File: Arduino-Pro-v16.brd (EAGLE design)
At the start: 100 x 80 mm, 41 parts, among them IC1 ATMEGA1281-16AU

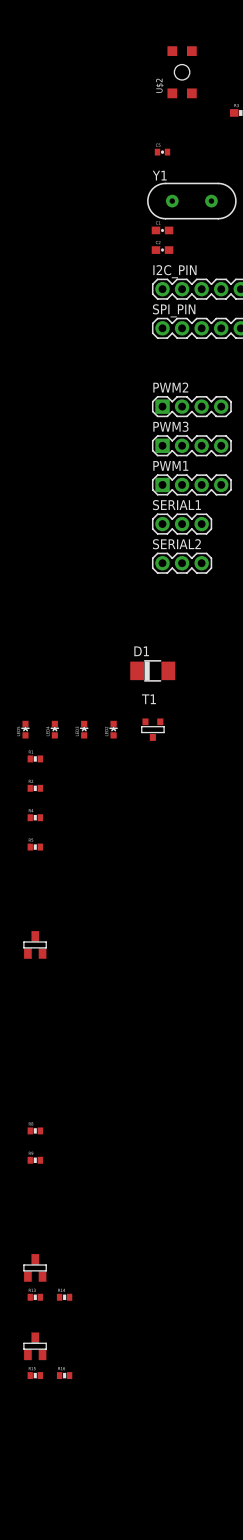
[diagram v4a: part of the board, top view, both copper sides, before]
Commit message: Added JTAG pins and smaller pushbutton
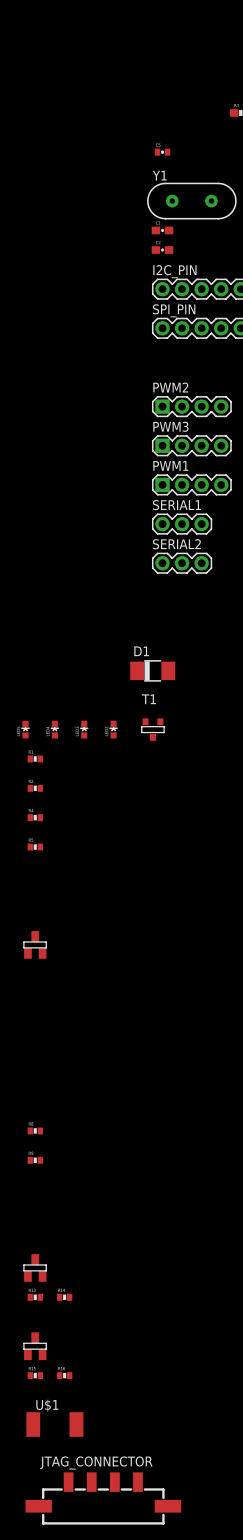
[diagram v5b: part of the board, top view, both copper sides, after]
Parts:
- removed U$2: TACTILE-SWITCH-7914G, GeekAmmo:7914G
- added JTAG_CONNECTOR: MICRO-FIT-4-SMD-PART, Connectors:MICRO-FIT-4-SMD
- added U$1: SWITCH, DiscreteComponents:SW_2512
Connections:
- new net JTTCK: IC1.57, JTAG_CONNECTOR.C4
- new net JTTDI: IC1.54, JTAG_CONNECTOR.C1
- new net JTTDO: IC1.55, JTAG_CONNECTOR.C2
- new net JTTMS: IC1.56, JTAG_CONNECTOR.C3
- net GND: now also U$1.1; no longer U$2.1, U$2.2
- net RESET: now also U$1.2; no longer U$2.3, U$2.4
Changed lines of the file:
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@@
 <?xml version="1.0" encoding="utf-8"?>
 <!DOCTYPE eagle SYSTEM "eagle.dtd">
-<eagle version="7.3.0">
+<eagle version="7.6.0">
 <drawing>
 <settings>
@@
 <element name="C5" library="SparkFun" package="0402-CAP" value="0.1uF" x="-55.88" y="-113.03"/>
 <element name="R3" library="SparkFun-Passives" package="0603-RES" value="10K" x="-45.72" y="-107.95"/>
-<element name="U$2" library="GeekAmmo" package="7914G" value="TACTILE-SWITCH-7914G" x="-54.61" y="-105.41"/>
 <element name="Y1" library="SparkFun-FreqCtrl" package="HC49US" value="" x="-52.07" y="-119.38"/>
 <element name="C1" library="SparkFun-Capacitors" package="0603-CAP" value="" x="-55.88" y="-123.19"/>
@@
 <element name="R15" library="SparkFun" package="0402-RES" value="10K" x="-72.39" y="-271.78"/>
 <element name="R16" library="SparkFun" package="0402-RES" value="10K" x="-68.58" y="-271.78"/>
+<element name="U$1" library="DiscreteComponents" package="SW_2512" value="SWITCH" x="-69.85" y="-278.13"/>
+<element name="JTAG_CONNECTOR" library="Connectors" package="MICRO-FIT-4-SMD" value="MICRO-FIT-4-SMD-PART" x="-73.66" y="-289.56">
+<attribute name="DIGIKEY-FEMALE-PN" value="WM2640CT-ND" x="-73.66" y="-289.56" size="1.778" layer="27" display="off"/>
+<attribute name="DIGIKEY-CONTACT-PN" value="WM1125CT-ND" x="-73.66" y="-289.56" size="1.778" layer="27" display="off"/>
+<attribute name="DIGIKEY-MALE-PN" value="WM1847-ND" x="-73.66" y="-289.56" size="1.778" layer="27" display="off"/>
+</element>
 </elements>
 <signals>
@@
 <contactref element="IC1" pad="22"/>
 <contactref element="C5" pad="1"/>
-<contactref element="U$2" pad="1"/>
-<contactref element="U$2" pad="2"/>
 <contactref element="IC1" pad="53"/>
 <contactref element="IC1" pad="63"/>
@@
 <contactref element="PCB1" pad="P$39"/>
 <contactref element="PCB1" pad="P$9"/>
+<contactref element="U$1" pad="1"/>
 <wire x1="-50.8" y1="-161.29" x2="-50.8" y2="-166.37" width="0" layer="19" extent="1-1"/>
 <wire x1="-45.72" y1="-135.89" x2="-50.8" y2="-161.29" width="0" layer="19" extent="1-1"/>
@@
 <wire x1="-55.03" y1="-123.19" x2="-55.03" y2="-125.73" width="0" layer="19" extent="1-1"/>
 <wire x1="-56.53" y1="-113.03" x2="-55.03" y2="-123.19" width="0" layer="19" extent="1-1"/>
-<wire x1="-54.61" y1="-105.41" x2="-56.53" y2="-113.03" width="0" layer="19" extent="1-1"/>
-<wire x1="-54.61" y1="-99.9236" x2="-54.61" y2="-105.41" width="0" layer="19" extent="1-1"/>
-<wire x1="-51.4985" y1="-89.0397" x2="-54.61" y2="-99.9236" width="0" layer="19" extent="1-1"/>
+<wire x1="-51.4985" y1="-89.0397" x2="-56.53" y2="-113.03" width="0" layer="19" extent="1-1"/>
 <wire x1="-54.6481" y1="-73.5203" x2="-51.4985" y2="-89.0397" width="0" layer="19" extent="1-1"/>
 <wire x1="-46.7741" y1="-73.5203" x2="-54.6481" y2="-73.5203" width="0" layer="19" extent="1-1"/>
@@
 <wire x1="-73.04" y1="-199.39" x2="-73.04" y2="-195.58" width="0" layer="19" extent="1-1"/>
 <wire x1="-73.04" y1="-203.2" x2="-73.04" y2="-199.39" width="0" layer="19" extent="1-1"/>
+<wire x1="-72.65" y1="-278.13" x2="-73.04" y2="-203.2" width="0" layer="19" extent="1-1"/>
 <wire x1="-13.2334" y1="-5.9182" x2="-46.7741" y2="-73.5203" width="0" layer="19" extent="1-1"/>
 <wire x1="-18.3134" y1="-3.3782" x2="-13.2334" y2="-5.9182" width="0" layer="19" extent="1-1"/>
@@
 <signal name="RESET">
 <contactref element="JP3" pad="5"/>
-<contactref element="U$2" pad="3"/>
-<contactref element="U$2" pad="4"/>
 <contactref element="R3" pad="1"/>
 <contactref element="IC1" pad="20"/>
-<wire x1="-52.07" y1="-99.9236" x2="-52.07" y2="-105.41" width="0" layer="19" extent="1-1"/>
-<wire x1="-46.57" y1="-107.95" x2="-52.07" y2="-105.41" width="0" layer="19" extent="1-1"/>
-<wire x1="-53.0733" y1="-89.0397" x2="-52.07" y2="-99.9236" width="0" layer="19" extent="1-1"/>
+<contactref element="U$1" pad="2"/>
+<wire x1="-53.0733" y1="-89.0397" x2="-46.57" y2="-107.95" width="0" layer="19" extent="1-1"/>
 <wire x1="-25.4" y1="3.81" x2="-53.0733" y2="-89.0397" width="0" layer="19" extent="1-1"/>
+<wire x1="-67.05" y1="-278.13" x2="-46.57" y2="-107.95" width="0" layer="19" extent="1-1"/>
 </signal>
 <signal name="SCK">
@@
 <wire x1="-20.8534" y1="-3.3782" x2="-23.3934" y2="-3.3782" width="0" layer="19" extent="1-1"/>
 </signal>
+<signal name="JTTDI">
+<contactref element="IC1" pad="54"/>
+<contactref element="JTAG_CONNECTOR" pad="C1"/>
+<wire x1="-68.06" y1="-285.605" x2="-47.5615" y2="-73.5203" width="0" layer="19" extent="1-1"/>
+</signal>
+<signal name="JTTDO">
+<contactref element="IC1" pad="55"/>
+<contactref element="JTAG_CONNECTOR" pad="C2"/>
+<wire x1="-65.06" y1="-285.605" x2="-48.3489" y2="-73.5203" width="0" layer="19" extent="1-1"/>
+</signal>
+<signal name="JTTMS">
+<contactref element="IC1" pad="56"/>
+<contactref element="JTAG_CONNECTOR" pad="C3"/>
+<wire x1="-62.06" y1="-285.605" x2="-49.1363" y2="-73.5203" width="0" layer="19" extent="1-1"/>
+</signal>
+<signal name="JTTCK">
+<contactref element="IC1" pad="57"/>
+<contactref element="JTAG_CONNECTOR" pad="C4"/>
+<wire x1="-59.06" y1="-285.605" x2="-49.9237" y2="-73.5203" width="0" layer="19" extent="1-1"/>
+</signal>
 </signals>

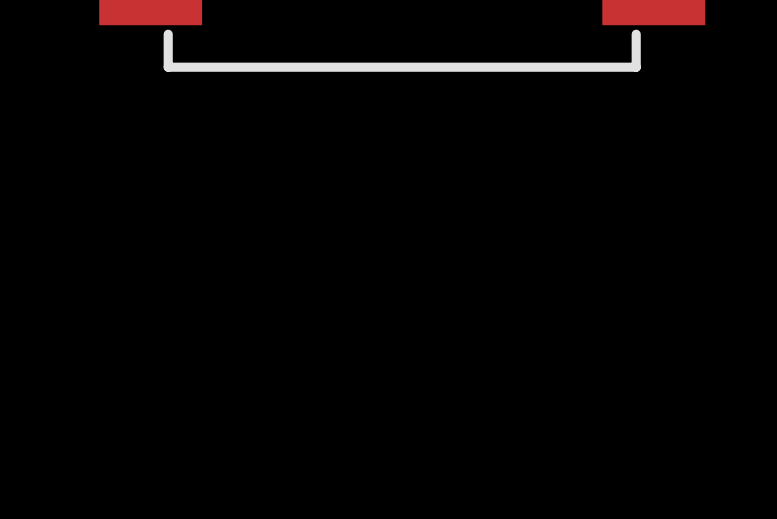
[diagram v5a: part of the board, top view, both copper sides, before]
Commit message: Added FTDI 3.3V programmer
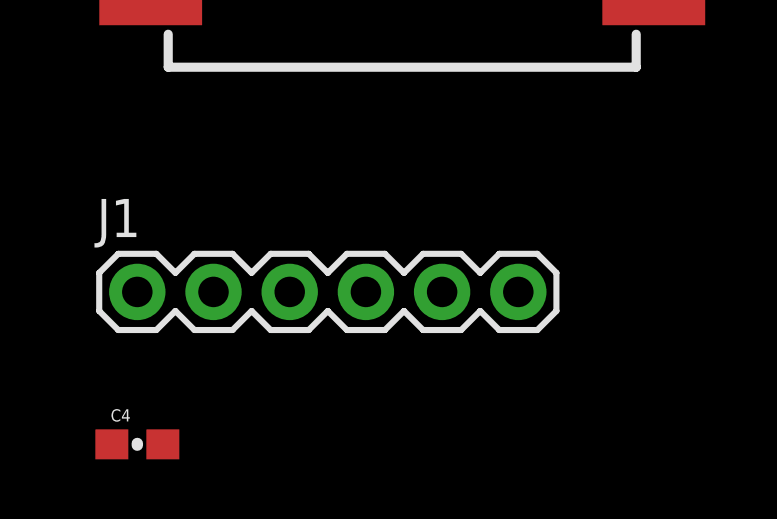
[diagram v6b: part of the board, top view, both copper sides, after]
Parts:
- added C4: (no value), SparkFun-Capacitors:0603-CAP
- added J1: FTDI Basic Programmer, SparkFun-Connectors:1X06
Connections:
- removed net VCCA: PCB1.P$2, PCB1.P$4
- new net DTR: C4.2, J1.1
- new net RXI: IC1.27, J1.3
- new net TX0: IC1.28, J1.2
- net 3V3: now also J1.4, PCB1.P$1, PCB1.P$17
- net 5VMISO: now also JP3.1
- net 5VMOSI: now also JP3.4
- net 5VROV: now also PCB1.P$2, PCB1.P$4
- net 5VSCK: now also JP3.3
- net GND: now also J1.5, J1.6
- net MISO: no longer JP3.1
- net MOSI: no longer JP3.4
- net RESET: now also C4.1
- net SCK: no longer JP3.3
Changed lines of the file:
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@@
 <attribute name="DIGIKEY-MALE-PN" value="WM1847-ND" x="-73.66" y="-289.56" size="1.778" layer="27" display="off"/>
 </element>
+<element name="J1" library="SparkFun-Connectors" package="1X06" value="FTDI Basic Programmer" x="-72.39" y="-298.45"/>
+<element name="C4" library="SparkFun-Capacitors" package="0603-CAP" value="" x="-72.39" y="-303.53"/>
 </elements>
 <signals>
@@
 <contactref element="PCB1" pad="P$9"/>
 <contactref element="U$1" pad="1"/>
+<contactref element="J1" pad="6"/>
+<contactref element="J1" pad="5"/>
 <wire x1="-50.8" y1="-161.29" x2="-50.8" y2="-166.37" width="0" layer="19" extent="1-1"/>
 <wire x1="-45.72" y1="-135.89" x2="-50.8" y2="-161.29" width="0" layer="19" extent="1-1"/>
@@
 <wire x1="-73.04" y1="-203.2" x2="-73.04" y2="-199.39" width="0" layer="19" extent="1-1"/>
 <wire x1="-72.65" y1="-278.13" x2="-73.04" y2="-203.2" width="0" layer="19" extent="1-1"/>
+<wire x1="-62.23" y1="-298.45" x2="-72.65" y2="-278.13" width="0" layer="19" extent="1-1"/>
+<wire x1="-59.69" y1="-298.45" x2="-62.23" y2="-298.45" width="0" layer="19" extent="1-1"/>
 <wire x1="-13.2334" y1="-5.9182" x2="-46.7741" y2="-73.5203" width="0" layer="19" extent="1-1"/>
 <wire x1="-18.3134" y1="-3.3782" x2="-13.2334" y2="-5.9182" width="0" layer="19" extent="1-1"/>
@@
 <contactref element="IC1" pad="20"/>
 <contactref element="U$1" pad="2"/>
+<contactref element="C4" pad="1"/>
 <wire x1="-53.0733" y1="-89.0397" x2="-46.57" y2="-107.95" width="0" layer="19" extent="1-1"/>
 <wire x1="-25.4" y1="3.81" x2="-53.0733" y2="-89.0397" width="0" layer="19" extent="1-1"/>
 <wire x1="-67.05" y1="-278.13" x2="-46.57" y2="-107.95" width="0" layer="19" extent="1-1"/>
+<wire x1="-73.24" y1="-303.53" x2="-67.05" y2="-278.13" width="0" layer="19" extent="1-1"/>
 </signal>
 <signal name="SCK">
-<contactref element="JP3" pad="3"/>
 <contactref element="SPI_PIN" pad="4"/>
-<wire x1="-27.94" y1="3.81" x2="-48.26" y2="-135.89" width="0" layer="19" extent="1-1"/>
 </signal>
 <signal name="N$38">
@@
 </signal>
 <signal name="MISO">
-<contactref element="JP3" pad="1"/>
 <contactref element="SPI_PIN" pad="2"/>
-<wire x1="-30.48" y1="3.81" x2="-53.34" y2="-135.89" width="0" layer="19" extent="1-1"/>
 </signal>
 <signal name="MOSI">
-<contactref element="JP3" pad="4"/>
 <contactref element="SPI_PIN" pad="3"/>
-<wire x1="-27.94" y1="6.35" x2="-50.8" y2="-135.89" width="0" layer="19" extent="1-1"/>
 </signal>
 <signal name="VCC">
@@
 <contactref element="D1" pad="A"/>
 <contactref element="T1" pad="3"/>
+<contactref element="PCB1" pad="P$2"/>
+<contactref element="PCB1" pad="P$4"/>
 <wire x1="-55.125" y1="-180.34" x2="-56.1594" y2="-186.944" width="0" layer="19" extent="1-1"/>
+<wire x1="-23.3934" y1="-3.3782" x2="-55.125" y2="-180.34" width="0" layer="19" extent="1-1"/>
+<wire x1="-20.8534" y1="-3.3782" x2="-23.3934" y2="-3.3782" width="0" layer="19" extent="1-1"/>
 </signal>
 <signal name="5VPROGRAMMER">
@@
 <contactref element="U$4" pad="2"/>
 <contactref element="IC1" pad="12"/>
+<contactref element="JP3" pad="4"/>
+<wire x1="-27.94" y1="6.35" x2="-57.2897" y2="-84.0359" width="0" layer="19" extent="1-1"/>
 <wire x1="-71.44" y1="-258.91" x2="-57.2897" y2="-84.0359" width="0" layer="19" extent="1-1"/>
 <wire x1="-69.23" y1="-261.62" x2="-71.44" y2="-258.91" width="0" layer="19" extent="1-1"/>
@@
 <contactref element="R13" pad="2"/>
 <contactref element="U$4" pad="1"/>
+<contactref element="PCB1" pad="P$1"/>
+<contactref element="PCB1" pad="P$17"/>
+<contactref element="J1" pad="4"/>
+<wire x1="-71.74" y1="-271.78" x2="-64.77" y2="-298.45" width="0" layer="19" extent="1-1"/>
 <wire x1="-72.39" y1="-266.87" x2="-71.74" y2="-271.78" width="0" layer="19" extent="1-1"/>
 <wire x1="-71.74" y1="-261.62" x2="-72.39" y2="-266.87" width="0" layer="19" extent="1-1"/>
@@
 <wire x1="-71.74" y1="-240.03" x2="-72.39" y2="-256.71" width="0" layer="19" extent="1-1"/>
 <wire x1="-72.39" y1="-214.8" x2="-71.74" y2="-240.03" width="0" layer="19" extent="1-1"/>
+<wire x1="-23.38" y1="-5.92" x2="-72.39" y2="-214.8" width="0" layer="19" extent="1-1"/>
+<wire x1="-3.0734" y1="-5.9182" x2="-23.38" y2="-5.92" width="0" layer="19" extent="1-1"/>
 </signal>
 <signal name="3V3MOSI">
@@
 <contactref element="U$3" pad="2"/>
 <contactref element="IC1" pad="13"/>
+<contactref element="JP3" pad="1"/>
+<wire x1="-30.48" y1="3.81" x2="-57.2897" y2="-84.8233" width="0" layer="19" extent="1-1"/>
 <wire x1="-71.44" y1="-217" x2="-57.2897" y2="-84.8233" width="0" layer="19" extent="1-1"/>
 <wire x1="-73.04" y1="-243.84" x2="-71.44" y2="-217" width="0" layer="19" extent="1-1"/>
@@
 <signal name="5VSCK">
 <contactref element="IC1" pad="11"/>
-</signal>
-<signal name="VCCA">
-<contactref element="PCB1" pad="P$2"/>
-<contactref element="PCB1" pad="P$4"/>
-<wire x1="-20.8534" y1="-3.3782" x2="-23.3934" y2="-3.3782" width="0" layer="19" extent="1-1"/>
+<contactref element="JP3" pad="3"/>
+<wire x1="-27.94" y1="3.81" x2="-57.2897" y2="-83.2485" width="0" layer="19" extent="1-1"/>
 </signal>
 <signal name="JTTDI">
@@
 <wire x1="-59.06" y1="-285.605" x2="-49.9237" y2="-73.5203" width="0" layer="19" extent="1-1"/>
 </signal>
+<signal name="RXI">
+<contactref element="IC1" pad="27"/>
+<contactref element="J1" pad="3"/>
+<wire x1="-67.31" y1="-298.45" x2="-47.5615" y2="-89.0397" width="0" layer="19" extent="1-1"/>
+</signal>
+<signal name="TX0">
+<contactref element="IC1" pad="28"/>
+<contactref element="J1" pad="2"/>
+<wire x1="-69.85" y1="-298.45" x2="-46.7741" y2="-89.0397" width="0" layer="19" extent="1-1"/>
+</signal>
+<signal name="DTR">
+<contactref element="C4" pad="2"/>
+<contactref element="J1" pad="1"/>
+<wire x1="-72.39" y1="-298.45" x2="-71.54" y2="-303.53" width="0" layer="19" extent="1-1"/>
+</signal>
 </signals>

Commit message: Added 3.3V linear regulator, delete logic level shifters
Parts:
- removed JP3: ISP, SparkFun:2X3
- removed R13, R14, R15, R16, R8, R9: 10K, SparkFun:0402-RES
- removed U$3, U$4, U$6: BSS138, DiscreteComponents:SOT-23-BSS138
- added IC2: MCP170312MB, linear:SOT89
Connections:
- removed net 5VCLK: R16.1, U$6.2
- removed net 5VMISO: IC1.13, JP3.1, R9.1, U$3.2
- removed net 5VMOSI: IC1.12, JP3.4, R14.1, U$4.2
- removed net 5VPROGRAMMER: JP3.2, T1.1
- removed net 5VSCK: IC1.11, JP3.3
- net 3V3: now also D1.A, IC2.3, T1.3; no longer R13.2, R15.2, R8.2, U$3.1, U$4.1, U$6.1
- net 3V3CLK: no longer R15.1, U$6.3
- net 3V3MISO: no longer R8.1, U$3.3
- net 3V3MOSI: no longer R13.1, U$4.3
- net 5VROV: now also IC2.2@1; no longer D1.A, T1.3
- net GND: now also IC2.1; no longer JP3.6
- net RESET: no longer JP3.5
- net RXI: now also IC1.2; no longer IC1.27
- net TX0: now also IC1.3; no longer IC1.28
- net VCC: no longer R14.2, R16.2, R9.2

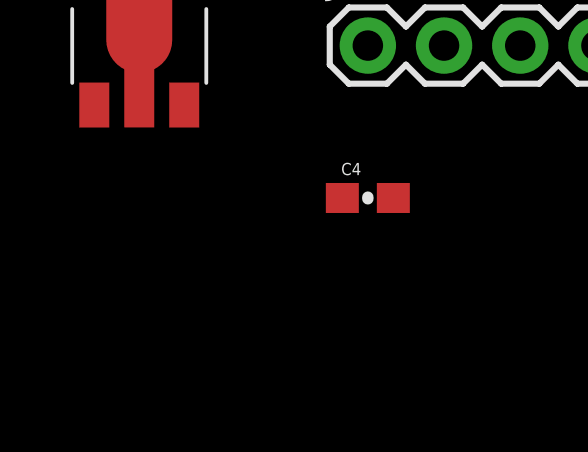
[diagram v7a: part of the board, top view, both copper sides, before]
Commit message: Added a pin out for alternate 3.3V power supply
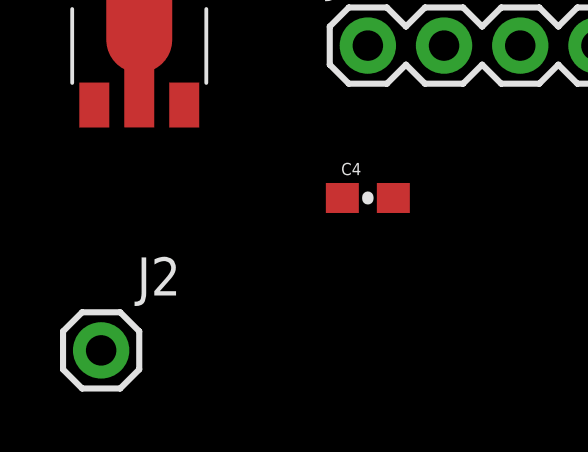
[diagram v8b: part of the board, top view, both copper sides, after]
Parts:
- added J2: (no value), SparkFun-Connectors:1X01
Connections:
- new net ALTVCC: J2.1, T1.1
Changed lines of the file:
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@@
 <element name="C4" library="SparkFun-Capacitors" package="0603-CAP" value="" x="-72.39" y="-303.53"/>
 <element name="IC2" library="linear" package="SOT89" value="MCP170312MB" x="-80.01" y="-298.45"/>
+<element name="J2" library="SparkFun-Connectors" package="1X01" value="" x="-81.28" y="-308.61"/>
 </elements>
 <signals>
@@
 <wire x1="-72.39" y1="-298.45" x2="-71.54" y2="-303.53" width="0" layer="19" extent="1-1"/>
 </signal>
+<signal name="ALTVCC">
+<contactref element="T1" pad="1"/>
+<contactref element="J2" pad="1"/>
+<wire x1="-81.28" y1="-308.61" x2="-57.1246" y2="-188.976" width="0" layer="19" extent="1-1"/>
+</signal>
 </signals>
